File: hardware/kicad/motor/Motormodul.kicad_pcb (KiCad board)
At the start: 2 copper layers, 64 x 60 mm, 53 parts, among them J100 Stapelstecker 2x20, J101 Kettenstecker, Buchse oben (S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, J102 Kettenstecker, Stift unten (S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, J103 Leistungsstecker, Buchse oben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, J104 Leistungsstecker, Stift unten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, J3 Notaus-Ruhestrom, J5 Motor-Klemme, Q1 IRFR5305, U1 DRV8876PWPR, U100 STM32C011F6P6, U101 SN74LVC1G175, U102 SN74LVC2G00DCUR, U103 SN74LVC1G08, U3 SN74LVC1G08, U4 PC817, U5 PC817, U6 SN74LVC1G06, U7 SN74LVC1G06

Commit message: Motormodul: freerouting-2.3.0-Umstieg, DSN-Splitter, Harfe, Vorverdrahtungsnetz
Der Verlege-Haenger aus dem Sicherungspunkt war keine einzelne kaputte
Koordinate, sondern eine Werkzeugschwaeche: KiCads DSN-Export
verschmilzt Vorverdrahtungs-Segmente reihenfolgeabhaengig zu
Mehrpunkt-Pfaden, und freerouting 2.2.4 haengt sich an manchen davon
auf -- die Bisektion fand deshalb vier scheinbar verschiedene
Ausloeser. Drei Massnahmen: 0/45/90-Gate gegen schiefe Segmente
(Rot-Nachweis am historischen 5-um-Fall), dsn_werkzeug.py spaltet
Mehrpunkt-Pfade (Rot-Nachweis inkl. Bruchkoordinaten-Luecke), und
freerouting 2.3.0 als JAR mit abgeschaltetem Optimierer und Fanout
(beides begruendet in autoroute.UMGEBUNG).

Dazu die Layout-Arbeit dieser Runde: Ladungspumpen-Caps als Harfe
gedreht, zehn Verbindungen vorverdrahtet (inkl. pre_vias() fuer
Lagenwechsel), Feinraster-Ausnahmen (Pad-Luft 0,15, Maskenraender
des TI-Footprints genullt), zwoelf Extra-Naehvias fuer die
Gussfragmente. DRC: 0 Verletzungen; offene Wackelkanten wuerfeln
noch (Schleife laeuft).

Co-Authored-By: Claude Opus 5 (1M context) <noreply@anthropic.com>
Claude-Session: https://claude.ai/code/session_01KDus95JJwCeRuwccgBWEi5
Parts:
- moved C10 3.52 mm to (46.3, 22.5), turned to 90 degrees
- moved C9 1.87 mm to (49.0, 24.6), turned to 90 degrees
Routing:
- net /+24V: track 1.80 -> 45.9 mm, vias 0 -> 2
- net /Out2: track 1.80 -> 44.7 mm
- net /ID0: track 0.00 -> 18.7 mm, vias 0 -> 2
- net /ID1: track 0.00 -> 16.4 mm, vias 0 -> 2
- net /NFAULT: track 0.00 -> 16.2 mm
- net 3V3: track 0.00 -> 14.4 mm, vias 0 -> 2
- net /SEL_OUT: track 0.50 -> 11.3 mm, vias 0 -> 2
- net /NRST: track 0.00 -> 8.54 mm
- net /VCP: track 0.00 -> 7.36 mm
- net /FLASH_MODE: track 0.00 -> 6.68 mm
- net /CPL: track 0.00 -> 4.83 mm
- net /CPH: track 0.00 -> 3.85 mm
- net GND: vias 22 -> 34

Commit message: Motormodul fertig: DRC 0/0, alle Proben gruen, Vertrag praezisiert
Die letzte Meile in Zahlen: DRC 0 Verletzungen und 0 unverbundene
Elemente, Steckerprobe komplett gruen (fuenf Stecker, Umriss,
Kennzeichnung, 46 Landepunkte, Lochbild), pcb_checks ohne Befund,
elf Testsuiten gruen.

Der Weg dahin:

* R5-Massekragen: Via-in-Pad statt Querbindung (die Bindung kostete
  den Router 3-5 Signale je Lauf); ebenso eine West-Ausleitung fuer
  U100-5 (MCU-GND) noerdlich der NRST-Bahn.
* Der C16-R15-Zug flog raus: er stammte aus der Zeit der
  3V3-Querwand und liess der /IPROPI-Ausfahrt nur 0,075 mm.
* Die letzte /+24V-Teilnetz-Luecke (D1/R16/R17-Gruppe gegen die
  Ost-Schiene) brauchte fuenf Anlaeufe von Hand -- die D1-Gasse ist
  von Out1-Rueckseite, SCHLEIFE_2-Diagonale und einem NOTAUS-Via
  belegt; die Bruecke laeuft jetzt ueber (34,8|40,0-40,5) und die
  Rueckseite bei y=40,0. Der Masseheiler setzte danach genau ein
  Heil-Via.
* C11-Abblockzweig auf Leistungsbreite (pcb_checks prueft je Netz
  und kennt keine stromlosen Zweige).
* ZWEI PROBEN-GROBHEITEN am Vertrag praezisiert, beide vom
  Motormodul aufgedeckt: die Verdrehtprobe mass Pads als KREIS mit
  max-Dimension-Radius (meldete 0,96 mm, real sind es 1,96) und
  misst jetzt den Rechteckabstand; der Pad-Schwerpunktvergleich
  kannte die asymmetrischen Loetpad-Ausleger der 2x02-SMD-Buchse
  nicht (PAD_SCHWERPUNKT_VERSATZ neu im Vertrag). Dazu 0,05 mm
  Messfehler in FOOTPRINT_HOF der Buchse korrigiert.

Co-Authored-By: Claude Fable 5 <noreply@anthropic.com>
Claude-Session: https://claude.ai/code/session_01KDus95JJwCeRuwccgBWEi5
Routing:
- net 3V3: track 14.4 -> 163.1 mm, vias 2 -> 8
- net /+24V: track 45.9 -> 121.7 mm, vias 2 -> 3
- net /SCHLEIFE_1: track 0.00 -> 54.2 mm, vias 0 -> 2
- net /PWR24V: track 0.00 -> 53.9 mm, vias 0 -> 2
- net /NOTAUS: track 0.00 -> 52.2 mm, vias 0 -> 2
- net /SCHLEIFE_2: track 0.00 -> 49.4 mm, vias 0 -> 4
- net /SEL_OUT: track 11.3 -> 56.3 mm, vias 2 -> 3
- net /IPROPI: track 0.00 -> 38.9 mm
- net /FLASH_RX: track 0.00 -> 35.7 mm, vias 0 -> 1
- net /FLASH_MODE: track 6.68 -> 41.8 mm, vias 0 -> 1
- net /Out1: track 1.80 -> 34.0 mm, vias 0 -> 1
- net /U4_LED_A: track 0.00 -> 31.5 mm, vias 0 -> 4
- net /SEL_IN: track 0.00 -> 28.0 mm, vias 0 -> 2
- net /U1_EN_IN1: track 0.00 -> 27.9 mm, vias 0 -> 4
- net /U1_NSLEEP: track 0.00 -> 24.2 mm, vias 0 -> 2
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
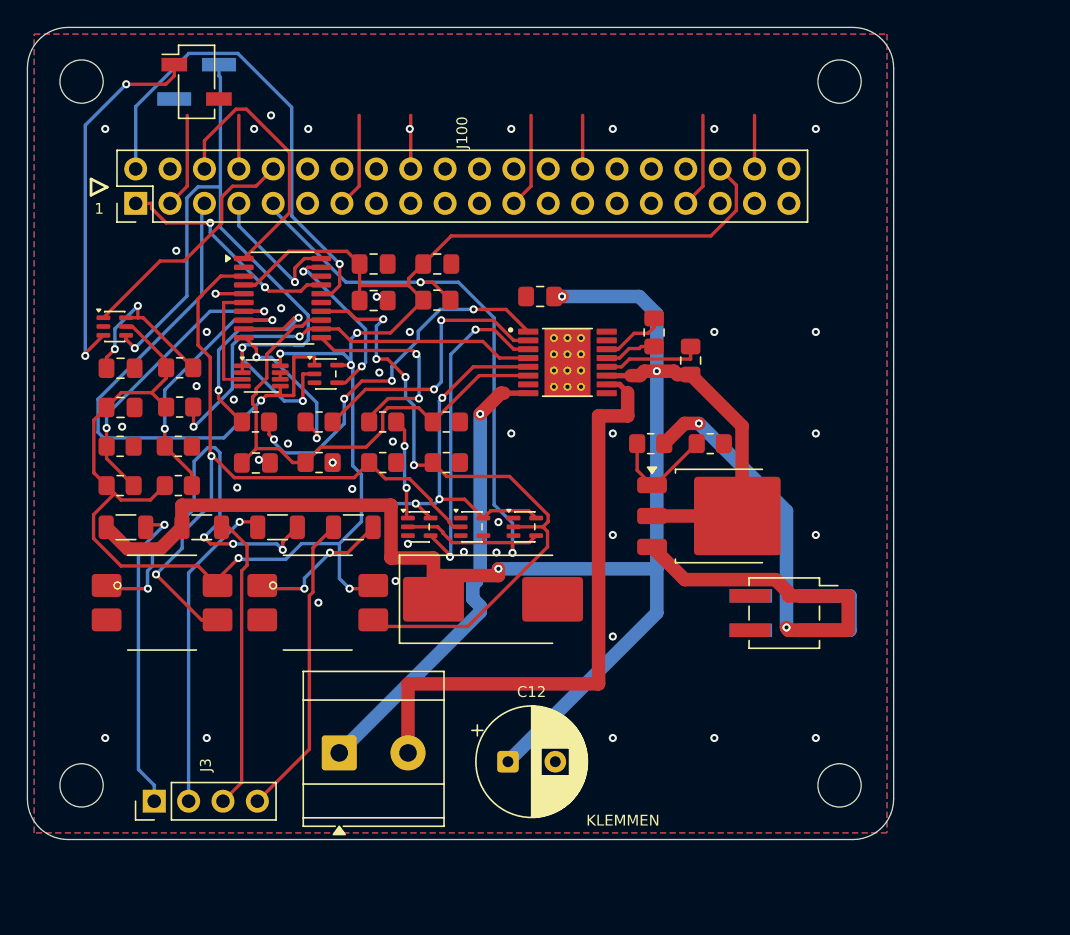
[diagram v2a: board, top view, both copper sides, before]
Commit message: Aufgabe 7b: Motormodul verlegt -- 25 DRC-Verletzungen auf 0, Vorverdrahtungs-Gate
Vorgefunden: 25 Verletzungen, 15 offene Verbindungen. Die Verletzungen
kamen NICHT vom Router, sondern aus der Vorverdrahtung selbst -- sieben
lange Querverbindungen, deren Koordinaten nie gegen die tatsaechlichen
Pad-Lagen gerechnet waren. Sie liefen mitten durch die Pads von J101
(Pad 2, GND) und J100 (Pad 1 und Pad 15), durch U1s eigenes GND-Pad 9
und durch U3-4. Gemessen mit einer DRC auf die gebaute Platine OHNE
jeden Router-Lauf: 21 Verletzungen, bevor freerouting startete.

Dieses Gate (bauen -> DRC, ohne Router, 40 Sekunden) ist jetzt der
Arbeitsschritt vor jedem Wuerfellauf. Es hat drei weitere
Vorverdrahtungs-Fehler gefangen, bevor sie einen Lauf gekostet haben.

spec_motor.py
  - Die sieben fehlerhaften Langstrecken ersatzlos entfernt. Grundsatz
    aus v1 wieder durchgehalten: vorverdrahtet wird nur, was der Router
    grundsaetzlich nicht kann.
  - Gestaffeltes Halsstueck-Paar an U1-10/U1-11 nachgezogen -- der eine
    v1-Fund, den v2 verloren hatte (zwei 1,0-mm-Bahnen an 0,65 mm
    entfernten Pads brauchen 1,2 mm Kappenabstand). /Out2 und /+24V
    blieben ohne es in JEDEM Lauf offen.
  - /Out2 ganz bis J5-2 und /+24V ganz bis C9-1 (ueber die Rueckseite um
    /Out2 herum) in Leistungsbreite festgelegt; Spuren gegen die
    Naehvia-Spalte x=45 gerechnet.
  - Ausfahrt von U1-12 (/VCP) vorverdrahtet, Masseanbindung von U6-3 und
    U7-3 (masseheiler fand dort in jedem Lauf keinen Heilpunkt).
  - Naehvia (45|21,25) per RULE_AREAS entfernt: es lag in der Mitte der
    einzigen Ausleitungsgasse des DRV8876 und kostete /VCP fuenf Laeufe.
  - 12 gezielte STITCH_EXTRA-Punkte, gegen das gebaute Brett gerechnet
    (>=0,50 mm zu Pads, >=0,90 zu Vias, >=0,45 zu Vorverdrahtung).

masseheiler.py: warf bei der ersten nicht heilbaren GND-Insel ALLES weg,
was es vorher geheilt hatte (Speichern passiert erst am Ende). Ein Lauf
mit restlos verlegter Platine kam so mit 11 offenen DRC-Poste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
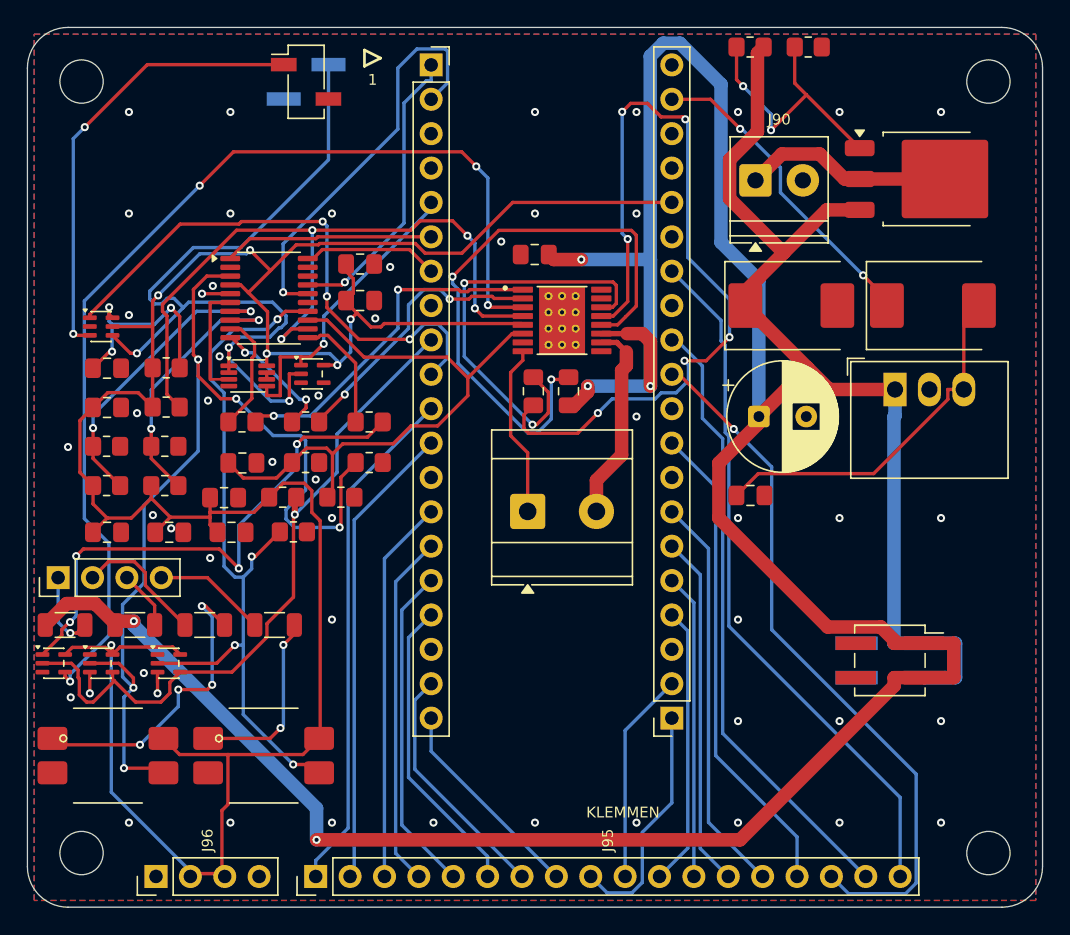
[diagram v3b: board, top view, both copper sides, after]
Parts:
- removed C12: 220u, CP_Radial_D8.0mm_P3.50mm
- removed D1: SMCJ30A, D_SMC_Handsoldering
- removed Q1: IRFR5305, TO-252-3_TabPin2
- removed R11, R12: 10k, R_0805_2012Metric_Pad1.20x1.40mm_HandSolder
- added C17: 100n, C_0805_2012Metric_Pad1.18x1.45mm_HandSolder, F.Cu at (5.88, 37.3)
- added C18: 100n, C_0805_2012Metric_Pad1.18x1.45mm_HandSolder, F.Cu at (10.5, 37.3)
- added C19: 100n, C_0805_2012Metric_Pad1.18x1.45mm_HandSolder, F.Cu at (15.1, 37.3)
- added C90: 220u, CP_Radial_D8.0mm_P3.50mm, F.Cu at (54.0, 28.8)
- added C91: 22u, C_0805_2012Metric_Pad1.18x1.45mm_HandSolder, F.Cu at (53.4, 34.6)
- added D90: SMCJ30A, D_SMC, F.Cu at (56.4, 20.6)
- added D91: SS36C, D_SMC, F.Cu at (66.9, 20.6)
- added J105: Stapelstecker rechts, Pico-Pins 21..40 (Buchse), PinSocket_1x20_P2.54mm_Vertical, F.Cu at (47.6, 51.0)
- added J90: Versorgung Eingang, TerminalBlock_Phoenix_PT-1,5-2-3.5-H_1x02_P3.50mm_Horizontal, F.Cu at (53.8, 11.3)
- added J95: Randpads GPIO, unbestueckt (THT-Loetpad), PinHeader_1x18_P2.54mm_Vertical, F.Cu at (21.3, 62.7)
- added J96: Randpads Versorgung: 2x 3V3 + 2x GND, unbestueckt (THT-Loet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, PinHeader_1x04_P2.54mm_Vertical, F.Cu at (9.50, 62.7)
- added Q90: IRFR5305, TO-252-3_TabPin2, F.Cu at (66.5, 11.2)
- added R90: 10k, R_0805_2012Metric_Pad1.20x1.40mm_HandSolder, F.Cu at (53.4, 1.45)
- added R91: 10k, R_0805_2012Metric_Pad1.20x1.40mm_HandSolder, F.Cu at (57.7, 1.45)
- added U90: K7805-1000R3, Converter_DCDC_RECOM_R-78B-2.0_THT, F.Cu at (64.1, 26.8)
- J100: value Stapelstecker 2x20 -> Stapelstecker links, Pico-Pins 1..20 (Buchse); footprint PinHeader_2x20_P2.54mm_Vertical -> PinSocket_1x20_P2.54mm_Vertical
- U6, U7: value SN74LVC1G06 -> SN74LVC1G07
- moved U6 29.2 mm to (5.45, 47.0)
- moved U3 28.8 mm to (1.95, 47.0)
- moved U7 28.2 mm to (10.4, 47.0)
- moved J100 24.1 mm to (29.8, 2.77), turned to 0 degrees
- moved C15 23.4 mm to (14.5, 34.7)
- moved J5 22.6 mm to (37.0, 35.8)
- moved R15 18.5 mm to (18.9, 34.7)
- moved J3 18.0 mm to (2.27, 40.6)
- moved R21 12.4 mm to (19.6, 37.3)
- moved H4 12.1 mm to (71.0, 61.0)
- moved U4 12.0 mm to (5.95, 53.8)
- moved U5 12.0 mm to (17.4, 53.8)
- moved H3 11.0 mm to (71.0, 4.00)
- moved C10 9.92 mm to (37.4, 26.9)
- moved R10 9.57 mm to (23.2, 34.7)
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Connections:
- J100 pad 11: unconnected-(J100-Pin_11-Pad11) -> /GP8
- J100 pad 12: unconnected-(J100-Pin_12-Pad12) -> /GP9
- J100 pad 14: unconnected-(J100-Pin_14-Pad14) -> /GP10
- J100 pad 15: unconnected-(J100-Pin_15-Pad15) -> /GP11
- J100 pad 16: unconnected-(J100-Pin_16-Pad16) -> /GP12
- J100 pad 17: unconnected-(J100-Pin_17-Pad17) -> /GP13
- J100 pad 19: unconnected-(J100-Pin_19-Pad19) -> /GP14
- J100 pad 20: unconnected-(J100-Pin_20-Pad20) -> /GP15
- J103 pad 1: /PWR24V -> /+24V
- J103 pad 3: /PWR24V -> /+24V
- J104 pad 1: /PWR24V -> /+24V
- J104 pad 3: /PWR24V -> /+24V
- U6 pad 1: (no net) -> unconnected-(U6-NC-Pad1)
- U7 pad 1: (no net) -> unconnected-(U7-NC-Pad1)
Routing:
- net /+24V: track 121.7 -> 270.1 mm, vias 3 -> 5
- net /CPH: track 3.85 -> 61.0 mm, vias 0 -> 6
- net /U1_NSLEEP: track 24.2 -> 78.1 mm, vias 2 -> 4
- net /PWR24V: track 53.9 -> 0.00 mm, vias 2 -> 0
- net /GP26: track 0.00 -> 52.5 mm, vias 0 -> 1
- net /GP28: track 0.00 -> 51.7 mm
- net /GP27: track 0.00 -> 45.8 mm
- net GND: track 46.0 -> 5.23 mm, vias 44 -> 51
- net 3V3: track 163.1 -> 203.7 mm, vias 8 -> 6
- net /GP8: track 0.00 -> 38.1 mm
- net /VCP: track 7.36 -> 43.8 mm, vias 0 -> 2
- net /GP22: track 0.00 -> 35.9 mm
- net /GP9: track 0.00 -> 34.5 mm
- net /NSLEEP_GATTER: track 7.46 -> 39.1 mm, vias 2 -> 4
- net /Out2: track 44.7 -> 14.8 mm
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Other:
- board size 64 x 60 mm -> 75 x 65 mm

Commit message: Aufgabe 7b: Motormodul auf der vertragstreuen Platzierung neu verlegt
Neu gebaut und neu verlegt, nachdem der B0-Fix beide Stapelreihen um
(+0,78|-0,50) mm auf die Vertragslage gezogen hat. 14 Wuerfellaeufe
(Laeufe n und p), bester Stand n2.

Stand:
  kicad-cli pcb drc --severity-error --exit-code-violations
    Found 0 violations
    Found 4 unconnected items
  davon EINE Netz-Luecke: /CPL  C10-2 <-> U1-14
  und drei GND-Inseln (masseheiler: F.Cu-Stuecke bei x 13,8..15,6 y
  26,3..27,1 und x 12,6..16,6 y 18,7..25,7; B.Cu-Stuecke bei
  x 47,0..49,3 y 43,6..48,8 und x 11,8..16,6 y 18,7..20,0).

  pcb_checks.py: 129 Vias, alle beidseitig angebunden; ANTENNE_FREI auf
  F.Cu kupferfrei.

  steckerprobe.py: alle SECHS Vertragsstecker auf der Vertragslage
  (stapel_links/rechts, kette, leistung), Umriss, Bohrungen, Lochbild
  und Kennzeichnung gruen -- erstmals, seit die Probe ueberhaupt laeuft.
  ROT bleibt allein die Verdreh-Kupferregel (16 Funde), s. Bericht.

Das Vorverdrahtungs-Gate (bauen + DRC OHNE Router) lief vor jedem Wurf
und war jedes Mal bei 0 Verletzungen -- die Vorverdrahtung hat den
Versatz der Stapelreihen unbeschadet ueberlebt, weil sie an U1 und am
MCU-Nest haengt, nicht an der Lage der Stapelreihen.

Die verbleibende /CPL-Luecke ist nicht Wuerfelpech, sondern die
Ueberbelegung des Ostkanals (Bedenken B1): durch die 4,39 mm zwischen
U1s Ostpadkante und der J105-Reihe muessen fuenf Netze, davon zwei in
Leistungsbreite. Nachgerechnet im Bericht, samt Nachweis, dass auch das
Verschieben von C9/C10 in den Kanal nicht aufgeht (0,06 mm Rest beim
Kondensator, 0,035 mm beim Halsstueck).

Co-Authored-By: Claude Fable 5 <noreply@anthropic.com>
Claude-Session: https://claude.ai/code/session_01KDus95JJwCeRuwccgBWEi5
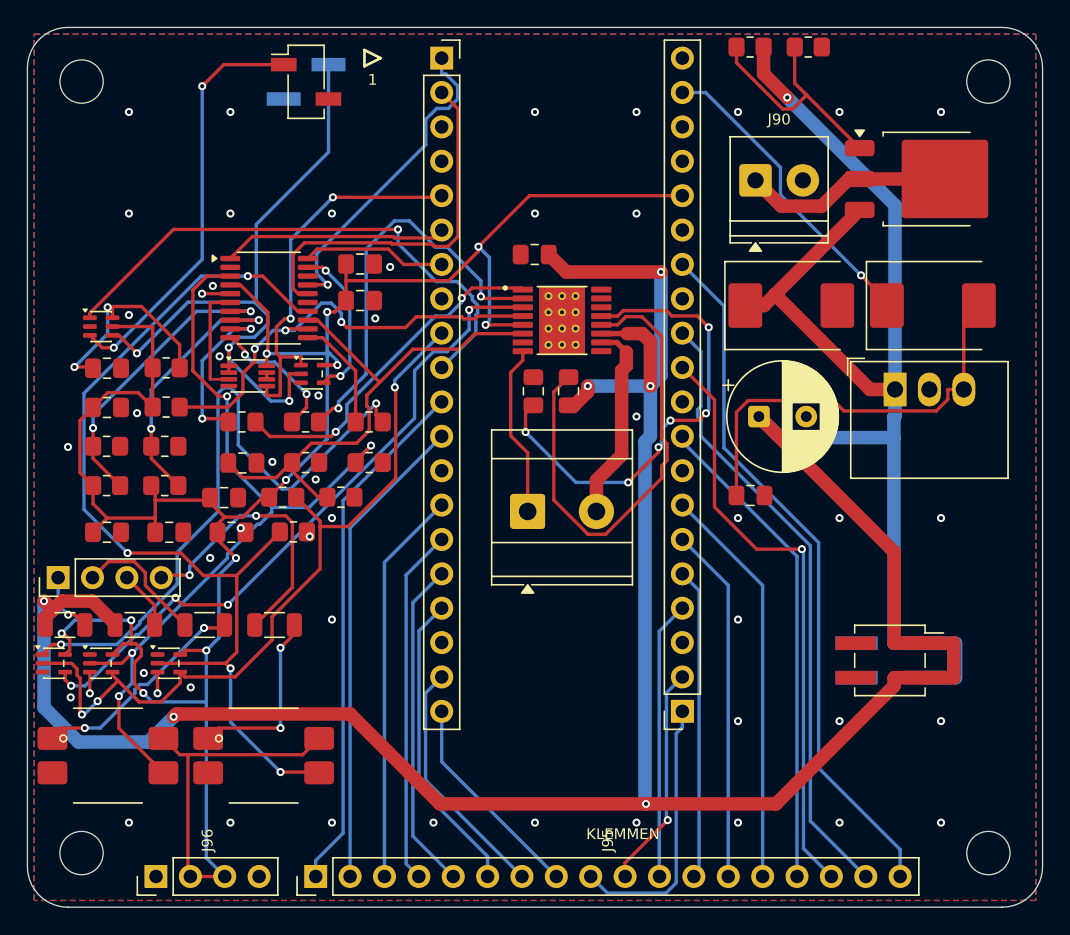
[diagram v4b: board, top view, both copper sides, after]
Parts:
- moved J100 0.93 mm to (30.6, 2.27)
- moved J105 0.93 mm to (48.4, 50.5)
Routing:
- net /CPL: track 31.1 -> 0.00 mm, vias 2 -> 0
- net /U1_NSLEEP: track 78.1 -> 49.5 mm
- net /CPH: track 61.0 -> 35.1 mm
- net /NFAULT: track 54.3 -> 33.2 mm, vias 4 -> 3
- net /SCHLEIFE_2: track 55.4 -> 72.1 mm
- net 3V3: track 203.7 -> 188.7 mm, vias 6 -> 11
- net /SCHLEIFE_1: track 76.1 -> 62.2 mm, vias 5 -> 4
- net /KREIS2_B: track 8.36 -> 20.9 mm, vias 0 -> 2
- net /BOOT0: track 0.00 -> 11.7 mm, vias 0 -> 2
- net /SEL_OUT: track 60.1 -> 49.3 mm
- net /NSLEEP_GATTER: track 39.1 -> 48.8 mm, vias 4 -> 2
- net /U1_PH_IN2: track 20.7 -> 29.9 mm
- net /GP26: track 52.5 -> 44.1 mm
- net /VCP: track 43.8 -> 36.4 mm, vias 2 -> 0
- net /U4_LED_A: track 22.9 -> 16.3 mm, vias 4 -> 2
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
